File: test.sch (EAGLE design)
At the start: 0 parts

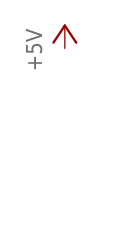
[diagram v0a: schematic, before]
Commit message: added GND
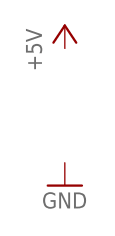
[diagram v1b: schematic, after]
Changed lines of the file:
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@@
 <parts>
 <part name="P+1" library="supply1" deviceset="+5V" device=""/>
+<part name="GND1" library="supply1" deviceset="GND" device=""/>
 </parts>
 <sheets>
@@
 <instances>
 <instance part="P+1" gate="1" x="25.4" y="86.36"/>
+<instance part="GND1" gate="1" x="25.4" y="68.58"/>
 </instances>
 <busses>

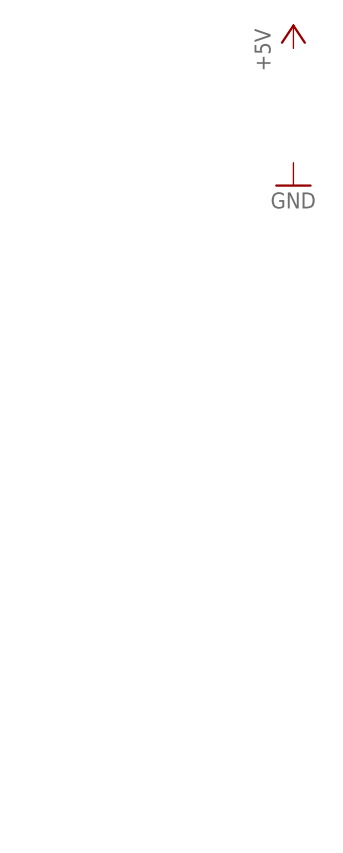
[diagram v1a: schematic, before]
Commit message: net 5V and GND, but 5V not connected in fact
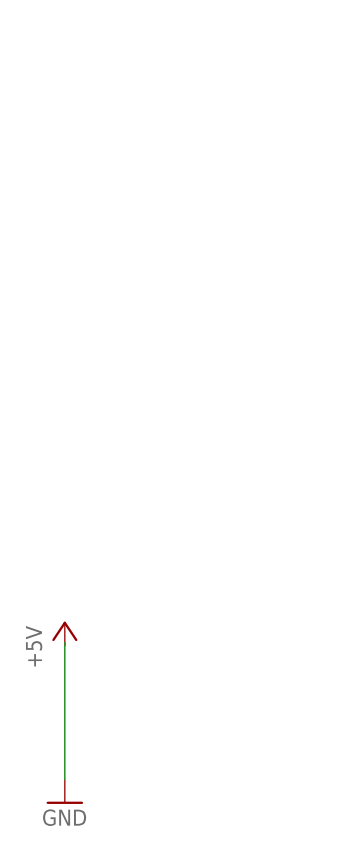
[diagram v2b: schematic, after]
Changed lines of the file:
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@@
 </plain>
 <instances>
-<instance part="P+1" gate="1" x="25.4" y="86.36"/>
-<instance part="GND1" gate="1" x="25.4" y="68.58"/>
+<instance part="P+1" gate="1" x="0" y="20"/>
+<instance part="GND1" gate="1" x="0" y="0"/>
 </instances>
 <busses>
 </busses>
 <nets>
+<net name="GND" class="0">
+<segment>
+<pinref part="GND1" gate="1" pin="GND"/>
+<wire x1="0" y1="17.78" x2="0" y2="2.54" width="0.1524" layer="91"/>
+</segment>
+</net>
 </nets>
 </sheet>

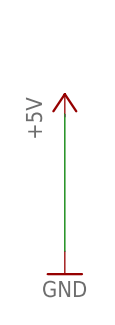
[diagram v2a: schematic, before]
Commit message: added resistor
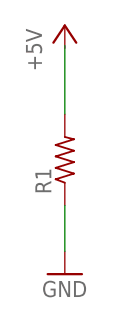
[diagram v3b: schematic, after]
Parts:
- added R1: (no value), rcl:R-US_0204/7
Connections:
- new net GND: R1.1
- new net N$1: R1.2
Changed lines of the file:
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@@
 <layer number="97" name="Info" color="7" fill="1" visible="yes" active="yes"/>
 <layer number="98" name="Guide" color="6" fill="1" visible="yes" active="yes"/>
+<layer number="99" name="SpiceOrder" color="5" fill="1" visible="yes" active="yes"/>
 </layers>
 <schematic xreflabel="%F%N/%S.%C%R" xrefpart="/%S.%C%R">
@@
 <part name="P+1" library="supply1" deviceset="+5V" device=""/>
 <part name="GND1" library="supply1" deviceset="GND" device=""/>
+<part name="R1" library="rcl" deviceset="R-US_" device="0204/7"/>
 </parts>
 <sheets>
@@
 </plain>
 <instances>
-<instance part="P+1" gate="1" x="0" y="20"/>
+<instance part="P+1" gate="1" x="0" y="27.62"/>
 <instance part="GND1" gate="1" x="0" y="0"/>
+<instance part="R1" gate="G$1" x="0" y="12.7" rot="R90"/>
 </instances>
 <busses>
 </busses>
 <nets>
+<net name="N$1" class="0">
+<segment>
+<pinref part="R1" gate="G$1" pin="2"/>
+<wire x1="0" y1="17.78" x2="0" y2="25.4" width="0.1524" layer="91"/>
+</segment>
+</net>
 <net name="GND" class="0">
 <segment>
+<pinref part="R1" gate="G$1" pin="1"/>
 <pinref part="GND1" gate="1" pin="GND"/>
-<wire x1="0" y1="17.78" x2="0" y2="2.54" width="0.1524" layer="91"/>
+<wire x1="0" y1="7.62" x2="0" y2="2.54" width="0.1524" layer="91"/>
 </segment>
 </net>
